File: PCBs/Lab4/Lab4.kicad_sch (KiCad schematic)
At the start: 9 parts, among them IC1 M0C1103QDDFRQ1, SW1 SW_SPST

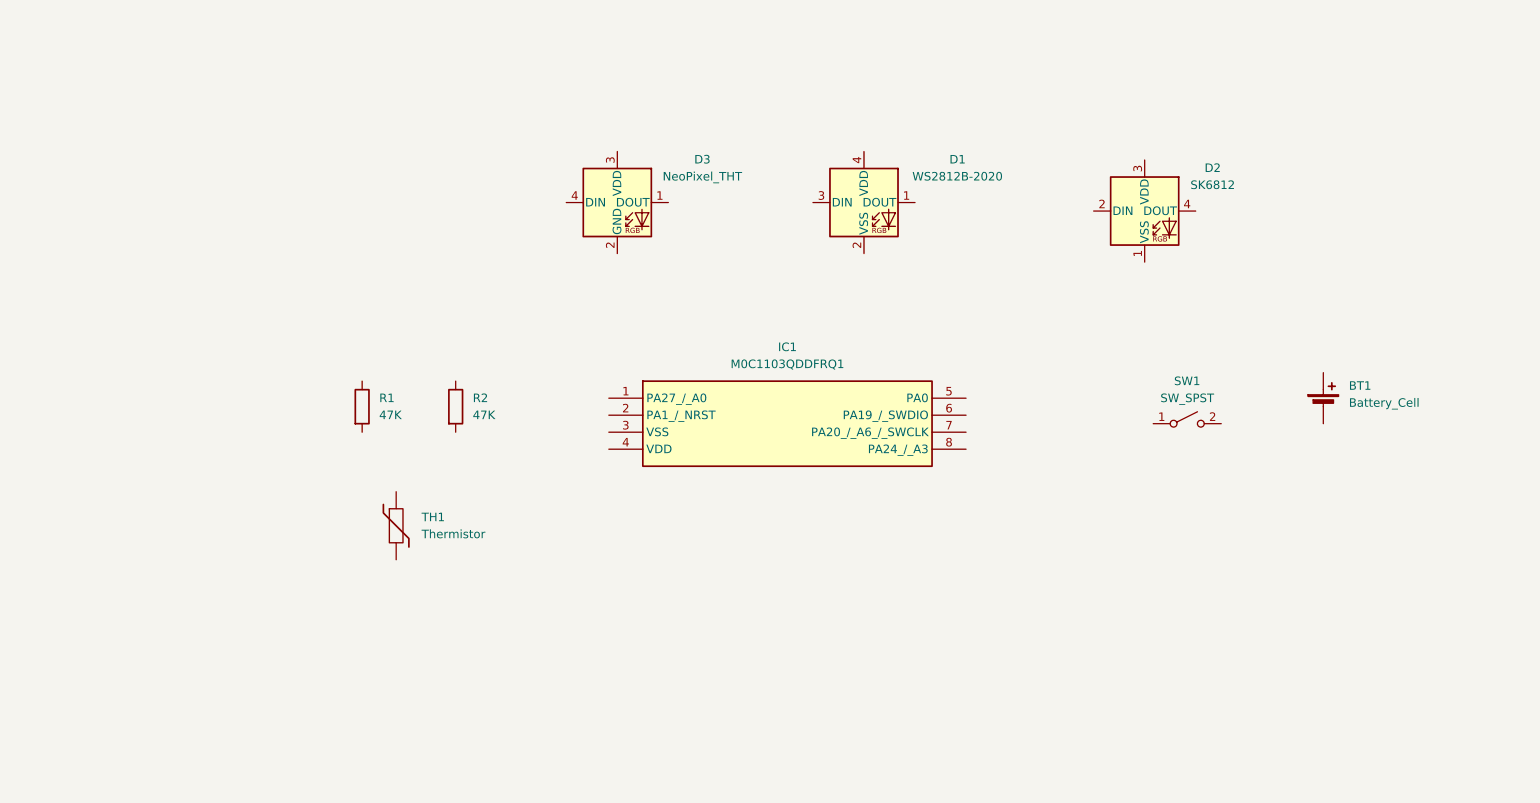
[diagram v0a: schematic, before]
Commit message: Updated Lab 4 with connections
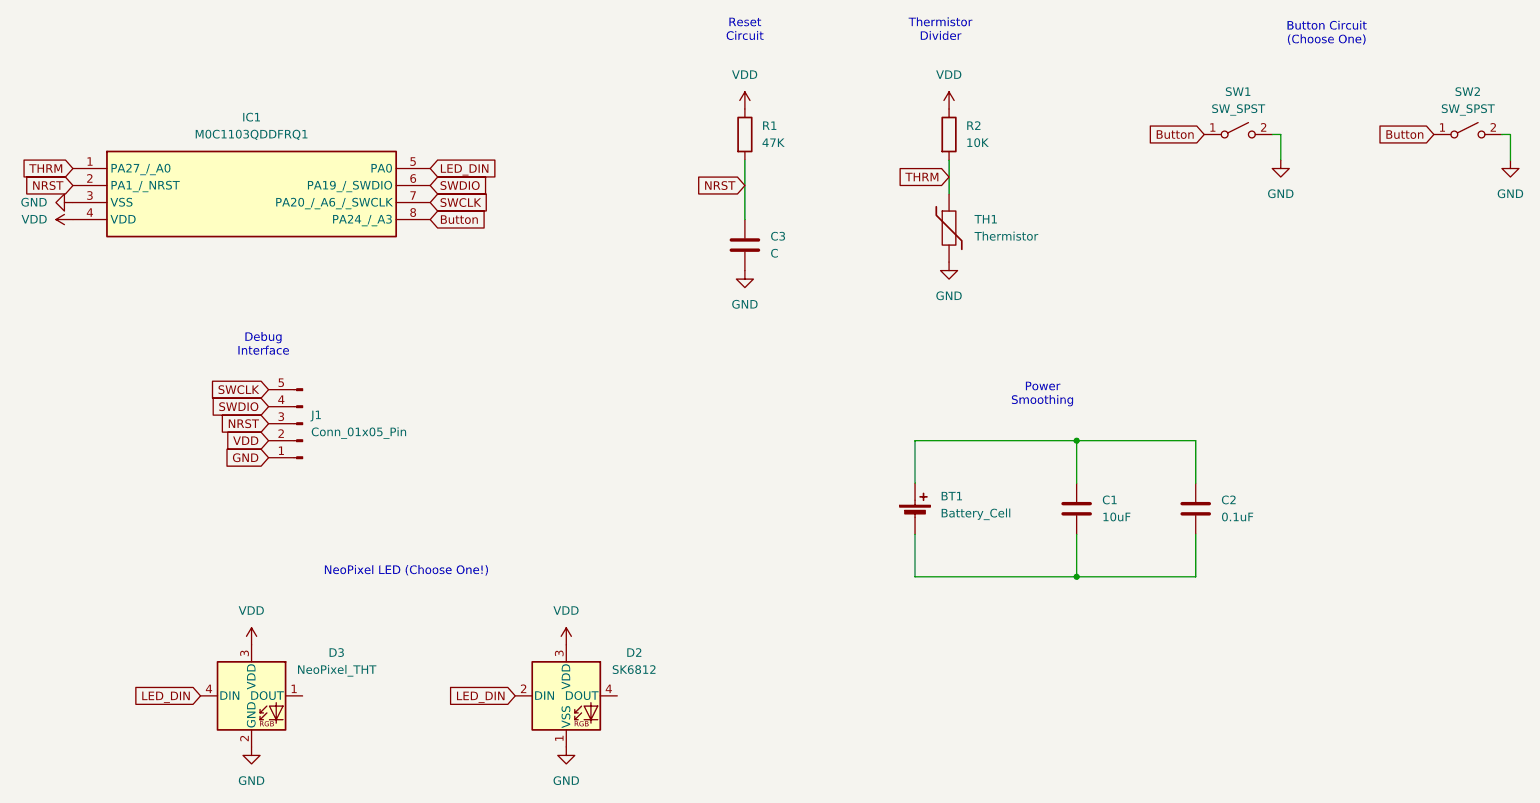
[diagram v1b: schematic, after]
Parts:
- removed D1: WS2812B-2020, LED_SMD:LED_WS2812B-2020_PLCC4_2.0x2.0mm, symbol LED:WS2812B-2020
- added C1: 10uF, Capacitor_SMD:C_1206_3216Metric_Pad1.33x1.80mm_HandSolder, symbol Device:C
- added C2: 0.1uF, Capacitor_SMD:C_1206_3216Metric_Pad1.33x1.80mm_HandSolder, symbol Device:C
- added C3: C, Capacitor_SMD:C_1206_3216Metric_Pad1.33x1.80mm_HandSolder, symbol Device:C
- added J1: Conn_01x05_Pin, Connector_PinHeader_2.54mm:PinHeader_1x05_P2.54mm_Vertical, symbol Connector:Conn_01x05_Pin
- added SW2: SW_SPST, Button_Switch_SMD:SW_SPST_PTS647_Sx50, symbol Switch:SW_SPST
- IC1: footprint SOT65P280X110-8N -> Package_TO_SOT_SMD:SOT-23-8
- R1: footprint (none) -> Resistor_SMD:R_1206_3216Metric_Pad1.30x1.75mm_HandSolder
- R2: value 47K -> 10K; footprint (none) -> Resistor_SMD:R_1206_3216Metric_Pad1.30x1.75mm_HandSolder
- TH1: footprint Resistor_SMD:R_1206_3216Metric -> Resistor_SMD:R_1206_3216Metric_Pad1.30x1.75mm_HandSolder
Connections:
- net Button: now reaches SW1.1 (A)
- net Button: now also IC1.8 (PA24_/_A3), SW2.1 (A)
- net GND: now reaches SW1.2 (B)
- net GND: now also D2.1 (VSS), D3.2 (GND), IC1.3 (VSS), TH1.2, C3.2, J1.1 (Pin_1), SW2.2 (B)
- net VDD: now reaches R1.1
- net VDD: now also D2.3 (VDD), D3.3 (VDD), IC1.4 (VDD), R2.1, J1.2 (Pin_2)
- net NRST: now reaches R1.2
- net NRST: now also IC1.2 (PA1_/_NRST), C3.1, J1.3 (Pin_3)
- net THRM: now reaches R2.2
- net THRM: now also IC1.1 (PA27_/_A0), TH1.1
- net LED_DIN: now reaches IC1.5 (PA0)
- net LED_DIN: now also D2.2 (DIN), D3.4 (DIN)
- net SWDIO: now reaches IC1.6 (PA19_/_SWDIO)
- net SWDIO: now also J1.4 (Pin_4)
- net SWCLK: now reaches IC1.7 (PA20_/_A6_/_SWCLK)
- net SWCLK: now also J1.5 (Pin_5)
- net at BT1.1 (+): now also C1.1, C2.1
- net at BT1.2 (-): now also C1.2, C2.2
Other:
- note added: "Button Circuit (Choose One)"
- note added: "Debug Interface"
- note added: "NeoPixel LED (Choose One!)"
- note added: "Power Smoothing"
- note added: "Reset Circuit"
- note added: "Thermistor Divider"
- moved on the sheet: BT1, D2, D3, R1, R2, SW1, TH1

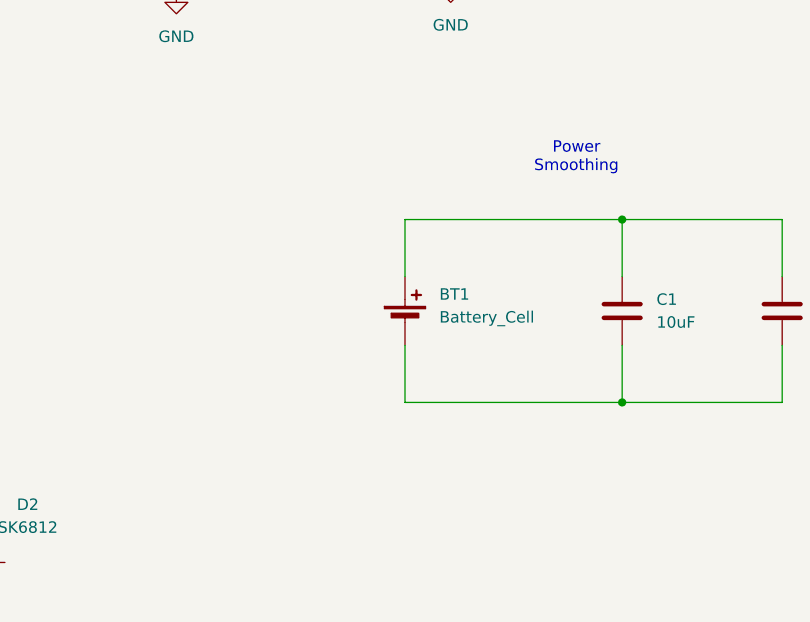
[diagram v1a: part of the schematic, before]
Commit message: Fixed missing VDD and GND
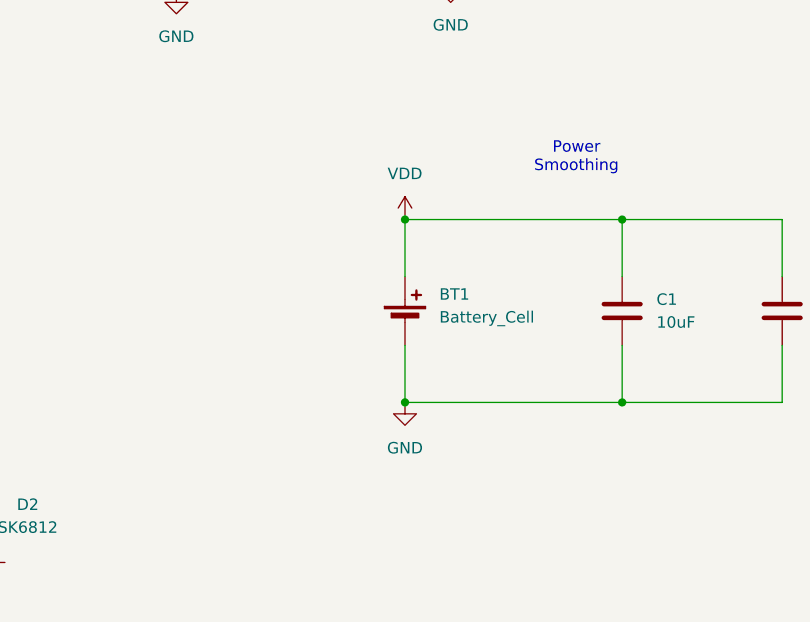
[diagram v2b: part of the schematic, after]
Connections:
- net GND: now also BT1.2 (-), C1.2, C2.2
- net VDD: now also BT1.1 (+), C1.1, C2.1
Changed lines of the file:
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@@
+	)
+	(junction
+		(at 154.94 88.9)
+		(diameter 0)
+		(color 0 0 0 0)
+	)
+	(junction
+		(at 154.94 109.22)
+		(diameter 0)
+		(color 0 0 0 0)
 	)
 	(junction
@@
 	)
 	(symbol
+		(lib_id "power:GND")
+		(at 154.94 109.22 0)
+		(unit 1)
+		(exclude_from_sim no)
+		(in_bom yes)
+		(on_board yes)
+		(dnp no)
+		(fields_autoplaced yes)
+		(property "Reference" "#PWR014"
+			(at 154.94 115.57 0)
+			(effects
+				(font
+					(size 1.27 1.27)
+				)
+				(hide yes)
+			)
+		)
+		(property "Value" "GND"
+			(at 154.94 114.3 0)
+			(effects
+				(font
+					(size 1.27 1.27)
+				)
+			)
+		)
+		(property "Footprint" ""
+			(at 154.94 109.22 0)
+			(effects
+				(font
+					(size 1.27 1.27)
+				)
+				(hide yes)
+			)
+		)
+		(property "Datasheet" ""
+			(at 154.94 109.22 0)
+			(effects
+				(font
+					(size 1.27 1.27)
+				)
+				(hide yes)
+			)
+		)
+		(property "Description" "Power symbol creates a global label with name \"GND\" , ground"
+			(at 154.94 109.22 0)
+			(effects
+				(font
+					(size 1.27 1.27)
+				)
+				(hide yes)
+			)
+		)
+		(pin "1"
+		)
+		(instances
+			(project "Lab4"
+				(path "/dbd6c5bc-048d-4ff3-939b-420beceeb6aa"
+					(reference "#PWR014")
+					(unit 1)
+				)
+			)
+		)
+	)
+	(symbol
 		(lib_id "Switch:SW_SPST")
 		(at 203.2 43.18 0)
@@
 					(unit 1)
 				)
+			)
+		)
+	)
+	(symbol
+		(lib_id "power:VDD")
+		(at 154.94 88.9 0)
+		(unit 1)
+		(exclude_from_sim no)
+		(in_bom yes)
+		(on_board yes)
+		(dnp no)
+		(fields_autoplaced yes)
+		(property "Reference" "#PWR05"
+			(at 154.94 92.71 0)
+			(effects
+				(font
+					(size 1.27 1.27)
+				)
+				(hide yes)
+			)
+		)
+		(property "Value" "VDD"
+			(at 154.94 83.82 0)
+			(effects
+				(font
+					(size 1.27 1.27)
+				)
+			)
+		)
+		(property "Footprint" ""
+			(at 154.94 88.9 0)
+			(effects
+				(font
+					(size 1.27 1.27)
+				)
+				(hide yes)
+			)
+		)
+		(property "Datasheet" ""
+			(at 154.94 88.9 0)
+			(effects
+				(font
+					(size 1.27 1.27)
+				)
+				(hide yes)
+			)
+		)
+		(property "Description" "Power symbol creates a global label with name \"VDD\""
+			(at 154.94 88.9 0)
+			(effects
+				(font
+					(size 1.27 1.27)
+				)
+				(hide yes)
+			)
+		)
+		(pin "1"
+		)
+		(instances
+			(project "Lab4"
+				(path "/dbd6c5bc-048d-4ff3-939b-420beceeb6aa"
+					(reference "#PWR05")
+					(unit 1)
+				)

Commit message: Switched through hole footprint for RGB LED
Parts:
- D3: footprint LED_THT:LED_D5.0mm-4_RGB -> LED_THT:LED_D5.0mm-4_RGB_Staggered_Pins
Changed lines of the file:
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@@
 			)
 		)
-		(property "Footprint" "LED_THT:LED_D5.0mm-4_RGB"
+		(property "Footprint" "LED_THT:LED_D5.0mm-4_RGB_Staggered_Pins"
 			(at 57.15 134.62 0)
 			(effects
